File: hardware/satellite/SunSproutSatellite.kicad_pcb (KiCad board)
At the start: 4 copper layers, 27.2 x 51.1 mm, 46 parts, among them J1 RJHSE5380_QwiicBusCompatible, J2 Conn_01x03, J3 Conn_01x03, J4 Conn_01x03, J5 Conn_01x03, J6 Conn_01x03, J7 Conn_01x04, J8 Qwiic, J9 Conn_01x04, U1 PCA9615DPZ, U2 ADS1115IDGS, U3 DS2482S-100+, U4 USBLC6-4SC6

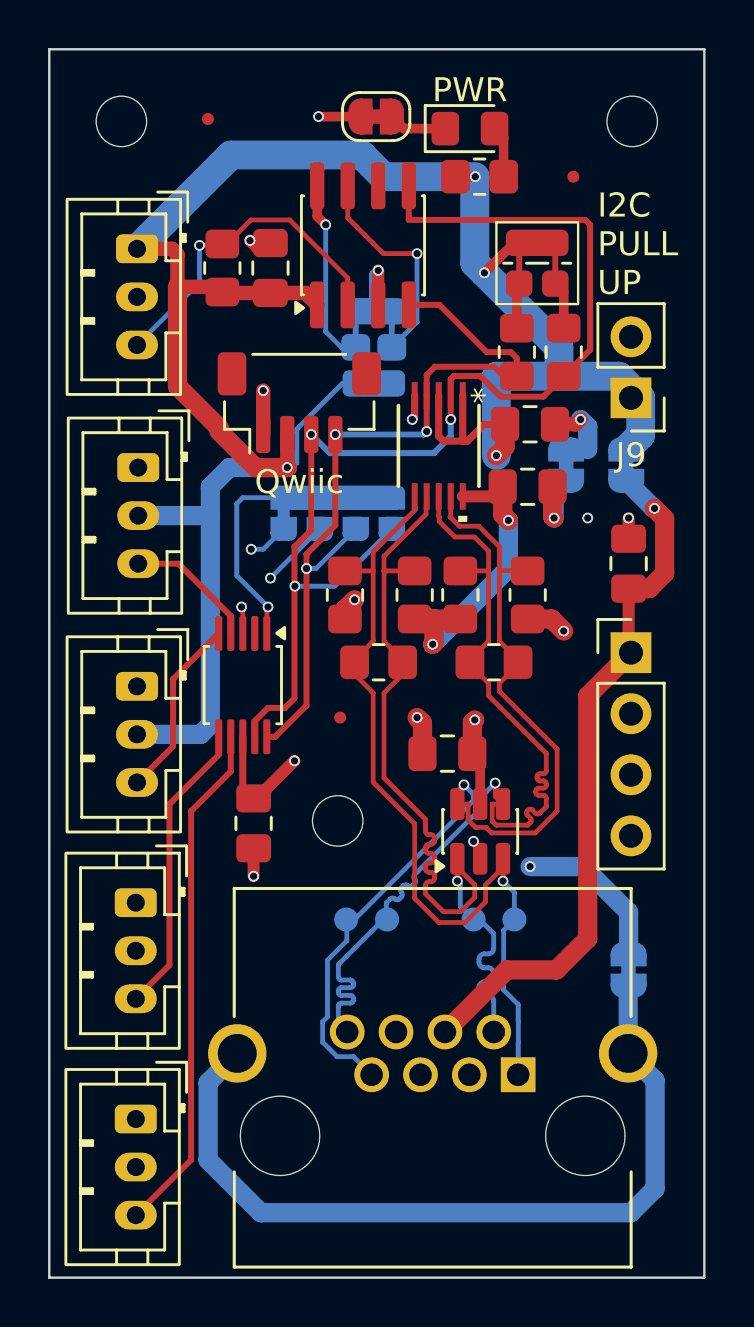
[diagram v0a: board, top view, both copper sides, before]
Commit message: hardware(satellite): stencil registration openings and wider traces
- Add F.Paste circles (Ø2.1 mm) on the three mounting holes for stencil
  registration
- Widen RJ45_GND_1 and SAT_3V3 narrow runs and other minor trace fixes

Co-Authored-By: Claude Sonnet 5.5 <noreply@anthropic.com>
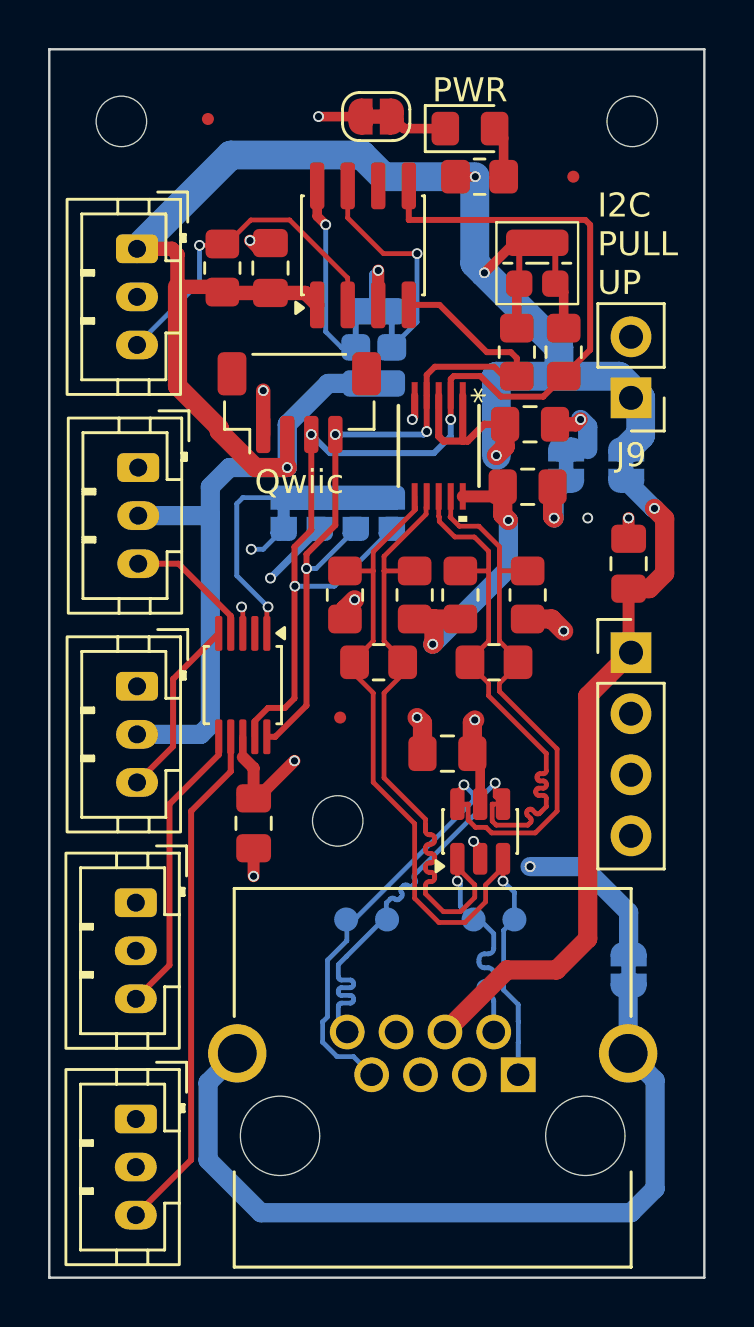
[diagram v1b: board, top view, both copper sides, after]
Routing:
- net SAT_3V3: track 148.2 -> 149.2 mm

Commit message: hardware(satellite): rev 1.1, larger address jumpers, qwiic moved clear of PCA9615
- JP1: enlarge footprint to 9.5 x 8.5 mm (2.0 mm row pitch, 2.0 x 1.2 mm
  pads) for easier solder and cut. Reorder pins 4/5 so the silkscreen and
  symbol read in address order: pin 4 = SDA = 0x4A, pin 5 = SCL = 0x4B.
  The silkscreen previously had 0x4A/0x4B swapped against the nets.
- JP16: enlarge footprint to 5.5 x 6.5 mm courtyard with larger pads.
- Move the qwiic port away from the PCA9615DPZ so hot-air rework of the
  buffer no longer melts the connector.
- Add the PCA9615 recommended TSSOP10 footprint and use it on U4.
- Add ohm signs to resistor values; update one termination value.
- Bump REV_NUM to 1.1.
- Update the ADS1115 and net-connection docs for the swapped JP1 pins.

Co-Authored-By: Claude Sonnet 5.5 <noreply@anthropic.com>
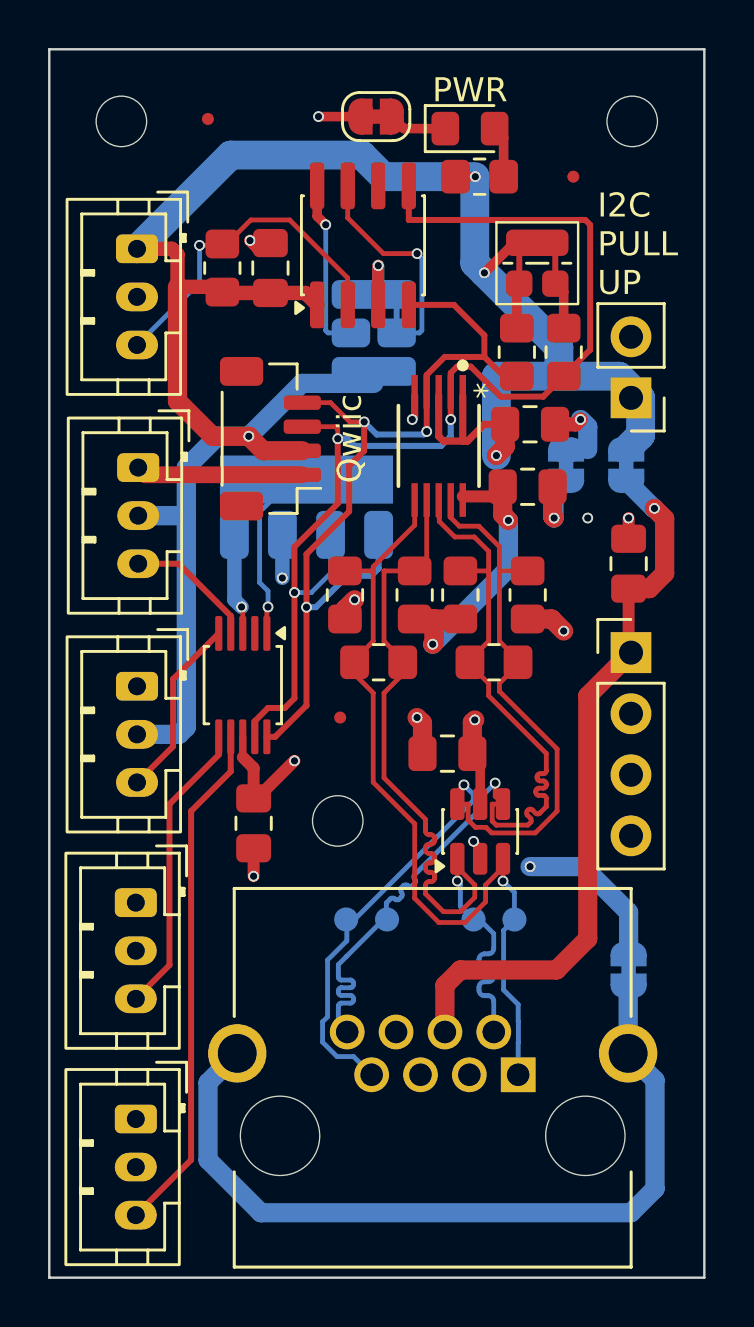
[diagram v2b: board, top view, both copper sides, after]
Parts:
- R1, R2: value 4.7k -> 4.7kΩ
- R10: value 120Ω -> 220Ω
- R3, R5, R6, R8: value 390 -> 390Ω
- R4, R7: value 100 -> 100Ω
- U1: footprint Snapeda:TSSOP10_SOT552-1_NXP-L -> project:TSSOP10_SOT552-1_NXP-Recommended
- moved G*** 6.27 mm to (123.1, 107.5)
- moved J8 1.92 mm to (109.2, 116.2), turned to 90 degrees
- moved JP1 1.32 mm to (110.7, 119.0)
- moved JP16 0.60 mm to (113.5, 111.8)
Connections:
- JP1 pad 4: SCL_LOCAL -> SDA_LOCAL
- JP1 pad 5: SDA_LOCAL -> SCL_LOCAL
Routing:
- net GND: track 15.5 -> 21.4 mm, vias 9 -> 7
- net SCL_LOCAL: track 33.5 -> 37.6 mm
- net SAT_3V3: track 149.2 -> 147.4 mm
- net ADDR_SEL: track 10.3 -> 11.9 mm
- net RJ45_VCC_1: track 56.8 -> 57.9 mm
- net DSCL_P: track 35.4 -> 34.7 mm
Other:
- board text added: "1-Wire"
- board text added: "CH1"
- board text added: "CH2"
- board text added: "CH3"
- board text added: "CH4"
